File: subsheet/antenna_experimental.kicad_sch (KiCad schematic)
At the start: 13 parts, among them J1 Conn_Coaxial, J904 Conn_Coaxial, U901 MASWSS0179

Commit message: Copy in component arrangement from SDMMC test design
Already had an efficient arrangement for the SPI flash chip, Clock
crystal, and Antenna.
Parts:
- renumbered AE901 to AE401, J1 to J401, J1 to J402, J1 to J403, J904 to J404, J1 to J405, U901 to U401
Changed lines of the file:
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@@
   (symbol (lib_id "Connector:Conn_Coaxial") (at 66.04 66.04 0) (mirror y) (unit 1)
     (in_bom yes) (on_board yes) (dnp no) (fields_autoplaced)
-    (property "Reference" "J1" (at 62.23 65.0632 0)
+    (property "Reference" "J401" (at 62.23 65.0632 0)
       (effects (font (size 1.27 1.27)) (justify left))
     )
@@
   (symbol (lib_id "Device:Antenna_Chip") (at 185.42 68.58 0) (unit 1)
     (in_bom yes) (on_board yes) (dnp no)
-    (property "Reference" "AE901" (at 190.5 64.77 0)
+    (property "Reference" "AE401" (at 190.5 64.77 0)
       (effects (font (size 1.27 1.27)) (justify left))
     )
@@
   (symbol (lib_id "Connector:Conn_Coaxial") (at 236.22 76.2 0) (unit 1)
     (in_bom yes) (on_board yes) (dnp no)
-    (property "Reference" "J1" (at 240.03 75.2232 0)
+    (property "Reference" "J405" (at 240.03 75.2232 0)
       (effects (font (size 1.27 1.27)) (justify left))
     )
@@
   (symbol (lib_id "Connector:Conn_Coaxial") (at 149.86 76.2 0) (unit 1)
     (in_bom yes) (on_board yes) (dnp no)
-    (property "Reference" "J1" (at 153.67 75.2232 0)
+    (property "Reference" "J402" (at 153.67 75.2232 0)
       (effects (font (size 1.27 1.27)) (justify left))
     )
@@
   (symbol (lib_id "power:GND") (at 66.04 71.12 0) (unit 1)
     (in_bom yes) (on_board yes) (dnp no) (fields_autoplaced)
-    (property "Reference" "#PWR0901" (at 66.04 77.47 0)
+    (property "Reference" "#PWR0401" (at 66.04 77.47 0)
       (effects (font (size 1.27 1.27)) hide)
     )
@@
   (symbol (lib_id "Connector:Conn_Coaxial") (at 195.58 76.2 0) (unit 1)
     (in_bom yes) (on_board yes) (dnp no)
-    (property "Reference" "J1" (at 199.39 75.2232 0)
+    (property "Reference" "J403" (at 199.39 75.2232 0)
       (effects (font (size 1.27 1.27)) (justify left))
     )
@@
   (symbol (lib_id "RF_Switch:MASWSS0179") (at 99.06 129.54 0) (unit 1)
     (in_bom yes) (on_board yes) (dnp no) (fields_autoplaced)
-    (property "Reference" "U901" (at 99.06 118.11 0)
+    (property "Reference" "U401" (at 99.06 118.11 0)
       (effects (font (size 1.27 1.27)))
     )
@@
   (symbol (lib_id "Connector:Conn_Coaxial") (at 228.6 66.04 0) (unit 1)
     (in_bom yes) (on_board yes) (dnp no) (fields_autoplaced)
-    (property "Reference" "J904" (at 232.41 65.0632 0)
-      (effects (font (size 1.27 1.27)) (justify left))
-    )
+    (property "Reference" "J404" (at 232.41 65.0632 0)
+      (effects (font (size 1.27 1.27)) (justify left))
+    )

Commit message: Position final few components
Removed one ESD diode arrray - experimental board, so not really needed,
with the exception of the USB lines.

Add and position 5V indicator LED

Finished wiring up the 5V buck-boost regulator
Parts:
- U401: now not fitted; now left out of the parts list
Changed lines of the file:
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@@
 		(at 99.06 129.54 0)
 		(unit 1)
-		(exclude_from_sim no)
-		(in_bom yes)
-		(on_board yes)
-		(dnp no)
+		(exclude_from_sim yes)
+		(in_bom no)
+		(on_board no)
+		(dnp yes)
 		(fields_autoplaced yes)
 		(property "Reference" "U401"

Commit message: Add order codes for all components
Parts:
- AE401, C302, J401, J402, J403, J404, J405, L301: JLCPCB_IGNORE (none) -> 1
- C301: LCSC (none) -> C1569
- C302: LCSC (none) -> C1561
- L301: LCSC (none) -> C162539
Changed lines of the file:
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@@
 			)
 		)
-		(property "LCSC" ""
+		(property "LCSC" "C162539"
+			(at 91.44 91.44 0)
+			(effects
+				(font
+					(size 1.27 1.27)
+				)
+				(hide yes)
+			)
+		)
+		(property "I2C address" ""
 			(at 91.44 91.44 0)
 			(effects
@@
 			)
 		)
+		(property "I2C address" ""
+			(at 66.04 66.04 0)
+			(effects
+				(font
+					(size 1.27 1.27)
+				)
+				(hide yes)
+			)
+		)
+		(property "JLCPCB_IGNORE" "1"
+			(at 66.04 66.04 0)
+			(effects
+				(font
+					(size 1.27 1.27)
+				)
+				(hide yes)
+			)
+		)
 		(pin "1"
 		)
@@
 			)
 		)
+		(property "I2C address" ""
+			(at 185.42 68.58 0)
+			(effects
+				(font
+					(size 1.27 1.27)
+				)
+				(hide yes)
+			)
+		)
+		(property "JLCPCB_IGNORE" "1"
+			(at 185.42 68.58 0)
+			(effects
+				(font
+					(size 1.27 1.27)
+				)
+				(hide yes)
+			)
+		)
 		(pin "1"
 		)
@@
 			)
 		)
+		(property "I2C address" ""
+			(at 236.22 76.2 0)
+			(effects
+				(font
+					(size 1.27 1.27)
+				)
+				(hide yes)
+			)
+		)
+		(property "JLCPCB_IGNORE" "1"
+			(at 236.22 76.2 0)
+			(effects
+				(font
+					(size 1.27 1.27)
+				)
+				(hide yes)
+			)
+		)
 		(pin "1"
 		)
@@
 			)
 		)
+		(property "I2C address" ""
+			(at 132.08 92.71 0)
+			(effects
+				(font
+					(size 1.27 1.27)
+				)
+				(hide yes)
+			)
+		)
+		(property "JLCPCB_IGNORE" "1"
+			(at 132.08 92.71 0)
+			(effects
+				(font
+					(size 1.27 1.27)
+				)
+				(hide yes)
+			)
+		)
 		(pin "1"
 		)
@@
 			)
 		)
+		(property "I2C address" ""
+			(at 149.86 76.2 0)
+			(effects
+				(font
+					(size 1.27 1.27)
+				)
+				(hide yes)
+			)
+		)
+		(property "JLCPCB_IGNORE" "1"
+			(at 149.86 76.2 0)
+			(effects
+				(font
+					(size 1.27 1.27)
+				)
+				(hide yes)
+			)
+		)
 		(pin "1"
 		)
@@
 			)
 		)
-		(property "LCSC" ""
+		(property "LCSC" "C1569"
+			(at 99.06 86.36 0)
+			(effects
+				(font
+					(size 1.27 1.27)
+				)
+				(hide yes)
+			)
+		)
+		(property "I2C address" ""
 			(at 99.06 86.36 0)
 			(effects
@@
 			)
 		)
-		(property "LCSC" ""
+		(property "LCSC" "C1561"
+			(at 106.68 91.44 0)
+			(effects
+				(font
+					(size 1.27 1.27)
+				)
+				(hide yes)
+			)
+		)
+		(property "I2C address" ""
 			(at 106.68 91.44 0)
 			(effects
@@
 			)
 		)
+		(property "I2C address" ""
+			(at 195.58 76.2 0)
+			(effects
+				(font
+					(size 1.27 1.27)
+				)
+				(hide yes)
+			)
+		)
+		(property "JLCPCB_IGNORE" "1"
+			(at 195.58 76.2 0)
+			(effects
+				(font
+					(size 1.27 1.27)
+				)
+				(hide yes)
+			)
+		)
 		(pin "1"
 		)
@@
 		)
 		(property "LCSC" ""
+			(at 132.08 101.6 0)
+			(effects
+				(font
+					(size 1.27 1.27)
+				)
+				(hide yes)
+			)
+		)
+		(property "I2C address" ""
+			(at 132.08 101.6 0)
+			(effects
+				(font
+					(size 1.27 1.27)
+				)
+				(hide yes)
+			)
+		)
+		(property "JLCPCB_IGNORE" "1"
 			(at 132.08 101.6 0)
 			(effects
@@
 			)
 		)
+		(property "I2C address" ""
+			(at 99.06 129.54 0)
+			(effects
+				(font
+					(size 1.27 1.27)
+				)
+				(hide yes)
+			)
+		)
 		(pin "1"
 		)
@@
 			)
 		)
+		(property "I2C address" ""
+			(at 228.6 66.04 0)
+			(effects
+				(font
+					(size 1.27 1.27)
+				)
+				(hide yes)
+			)
+		)
+		(property "JLCPCB_IGNORE" "1"
+			(at 228.6 66.04 0)
+			(effects
+				(font
+					(size 1.27 1.27)
+				)
+				(hide yes)
+			)
+		)
 		(pin "1"
 		)
@@
 			(at 139.7 68.58 0)
 			(effects
+				(font
+					(size 1.27 1.27)
+				)
+				(hide yes)
+			)
+		)
+		(property "I2C address" ""
+			(at 139.7 68.58 0)
+			(effects

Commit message: Silkscreen work. Edit tittle block/version number
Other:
- company: (none) -> (c) Vincent Dalstra
- title: (none) -> Untitled 4-layer JLCPCB
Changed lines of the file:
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@@
 	(generator_version "8.0")
 	(paper "A4")
+	(title_block
+		(title "Untitled 4-layer JLCPCB")
+		(date "2024-06-14")
+		(rev "1.0.0")
+		(company "(c) Vincent Dalstra")
+	)
 	(junction
 		(at 132.08 86.36)

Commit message: Move all subsheets into 'main' subsheet, below root
Keeping all the subsheets in a dedicated 'subsheet' folder makes things
much, much neater. However, specifying filepaths for subsheets has an
interesting problem; they use paths RELATIVE TO THE PARENT SHEET.

The consequence of is that if a subsheet is part of the root sheet, it
needs to be prefixed with 'subsheet/', but NOT if it's further down.
This inconsistency can be resolved by having a single 'main' sheet at
the top that doesn't move.

It's also useful to have a top-level space to put down changelogs,
descriptions etc.
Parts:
- renumbered AE401 to AE501, C301 to C501, C302 to C502, C302 to C503, E301 to E501, J401 to J501, J402 to J502, J403 to J503, J404 to J504, J405 to J505, L301 to L501, L301 to L502, U401 to U501

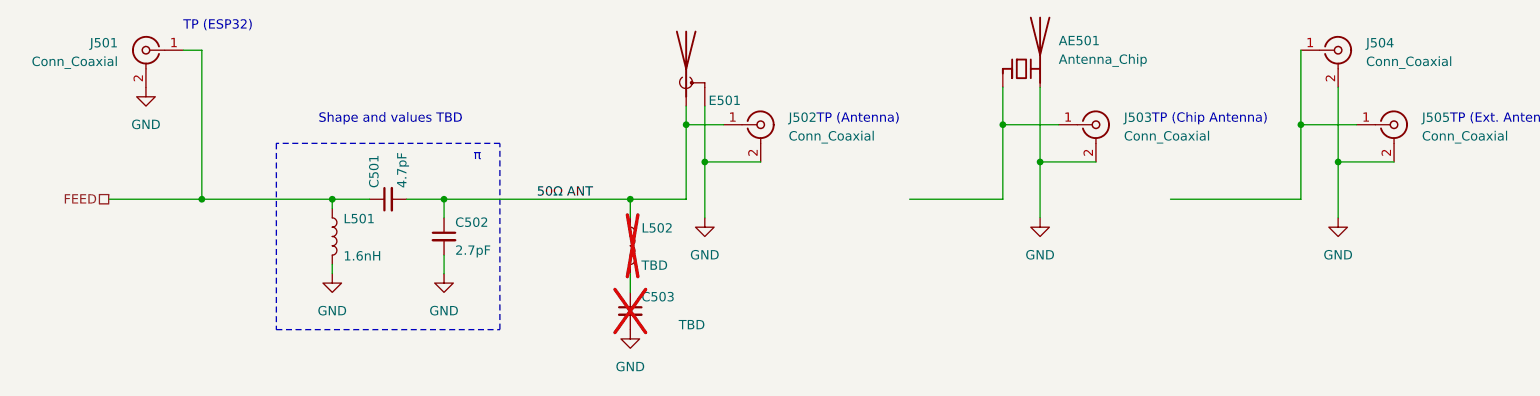
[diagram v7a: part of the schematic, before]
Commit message: Update file format to KiCAD 9.0
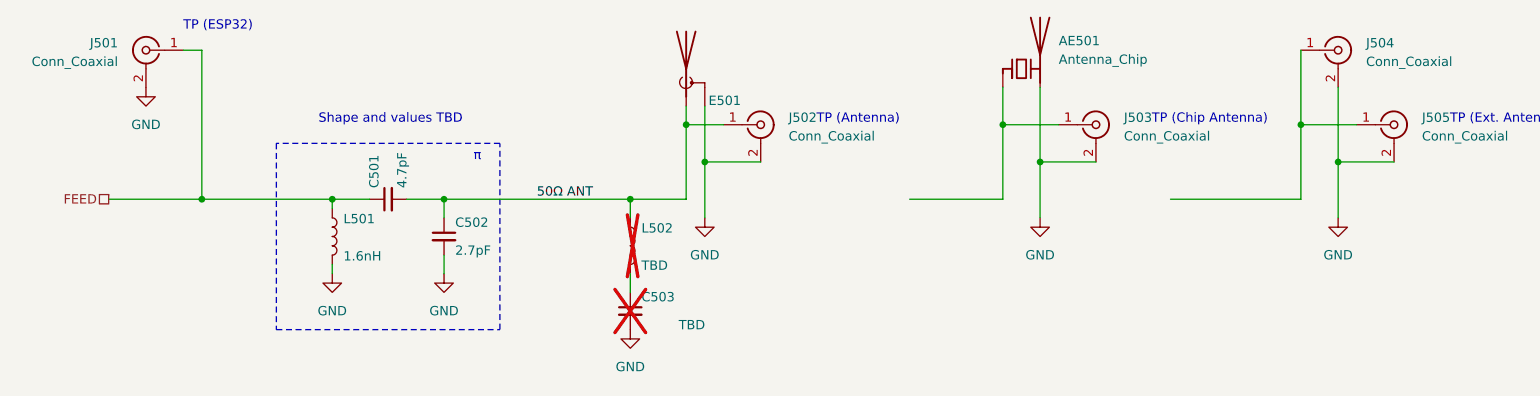
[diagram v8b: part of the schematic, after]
